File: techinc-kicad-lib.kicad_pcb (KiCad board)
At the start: 2 copper layers, 68.6 x 53.3 mm, 17 parts, among them IC1 WS2801, IC2 MAX490, IC3 WS2811, U1 ESP-01, U10 ARDUINOSHIELD, U11 ARDUINOSHIELD, U12 ARDUINOSHIELD, U13 IN-14, U2 ESP-03, U3 WS2812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

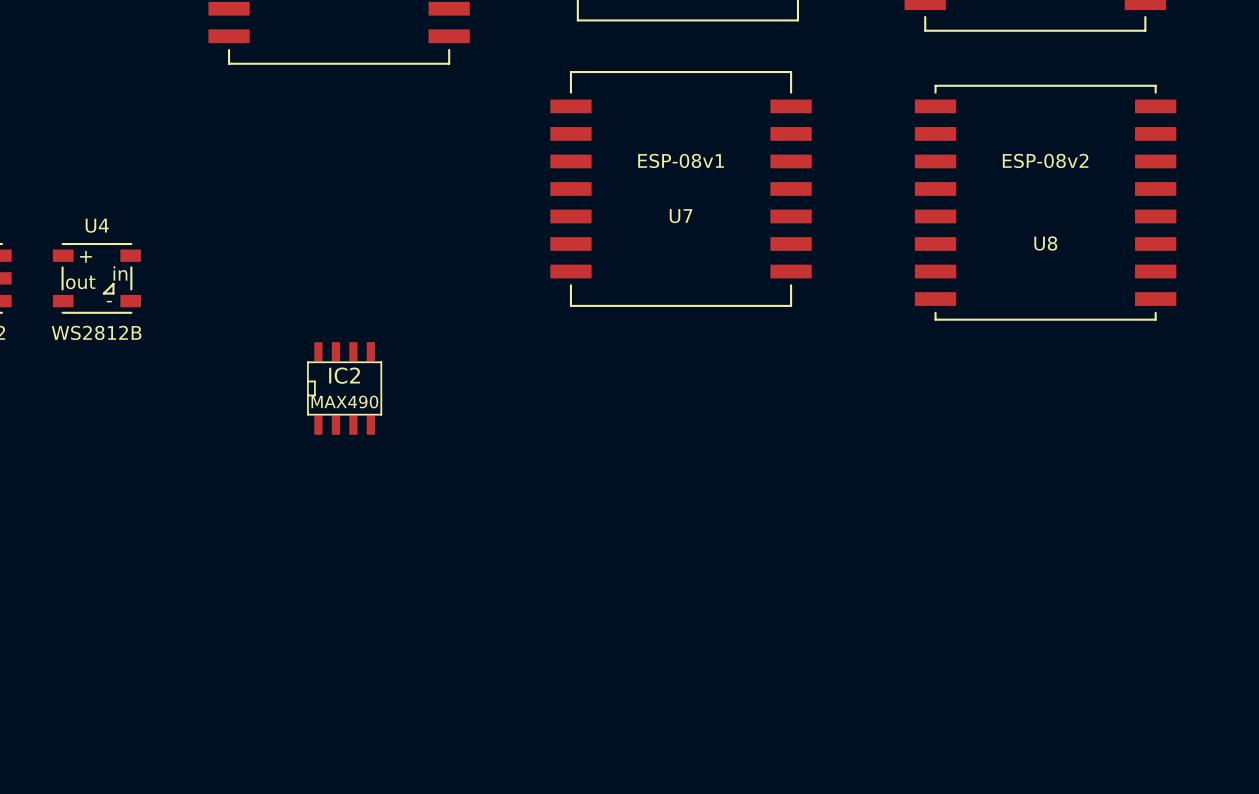
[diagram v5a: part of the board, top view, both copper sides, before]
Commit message: fix esp pinout, add SOT voltage regulator
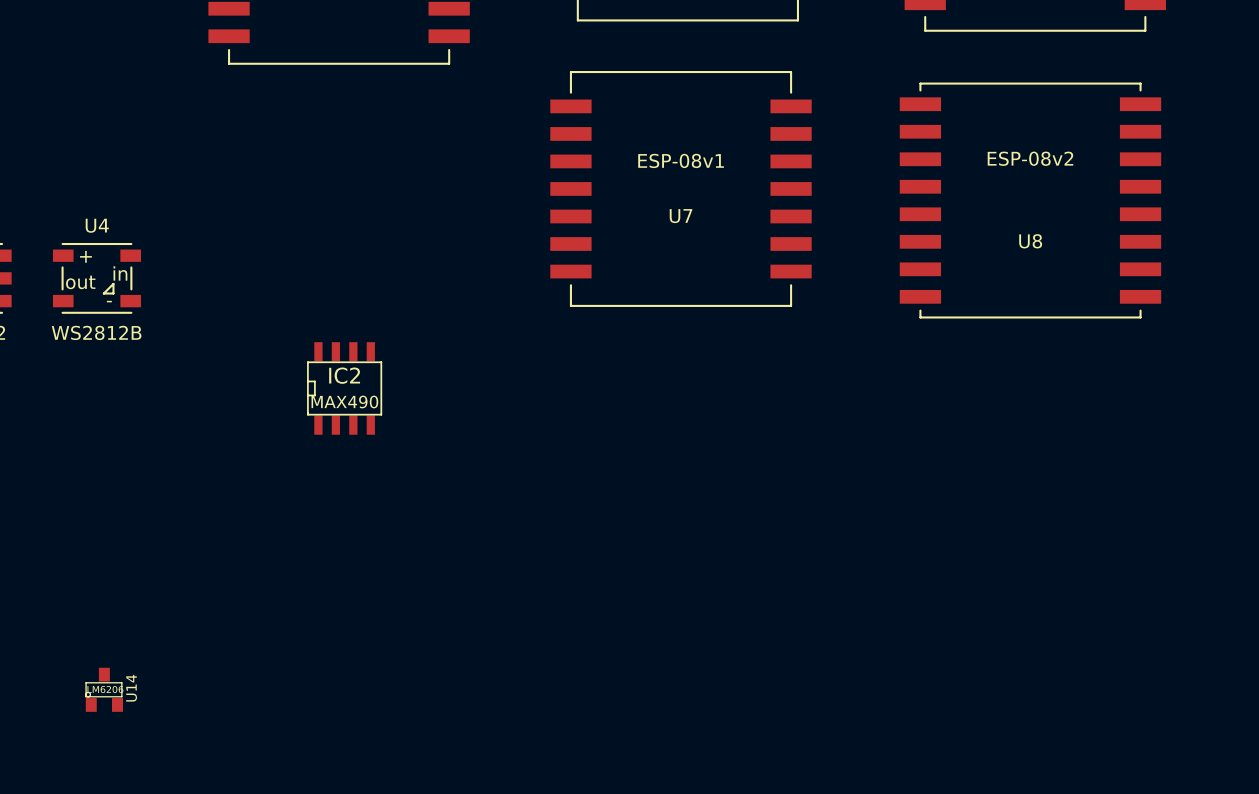
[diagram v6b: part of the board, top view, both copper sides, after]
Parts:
- added U14: LM6206, SOT23, F.Cu at (53.3, 88.9)
- moved U8 1.11 mm to (120.7, 53.3)
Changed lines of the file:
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@@
     (tracks 0)
     (zones 0)
-    (modules 17)
+    (modules 18)
     (nets 1)
   )
@@
     (mod_text_size 1 1)
     (mod_text_width 0.15)
-    (pad_size 1.5 1.5)
-    (pad_drill 1.016)
+    (pad_size 2 1)
+    (pad_drill 0)
     (pad_to_mask_clearance 0)
     (aux_axis_origin 0 0)
@@
     )
   )
-  (module ESP-08v2 (layer F.Cu)
-    (at 121.75 53.5)
-    (fp_text reference U8 (at 0 3) (layer F.SilkS)
-      (effects (font (size 1 1) (thickness 0.15)))
-    )
-    (fp_text value ESP-08v2 (at 0 -3) (layer F.SilkS)
-      (effects (font (size 1 1) (thickness 0.15)))
-    )
-    (fp_line (start -8 -8) (end -8 -8.5) (layer F.SilkS) (width 0.15))
-    (fp_line (start -8 -8.5) (end 8 -8.5) (layer F.SilkS) (width 0.15))
-    (fp_line (start 8 -8.5) (end 8 -8) (layer F.SilkS) (width 0.15))
-    (fp_line (start -8 8) (end -8 8.5) (layer F.SilkS) (width 0.15))
-    (fp_line (start -8 8.5) (end 8 8.5) (layer F.SilkS) (width 0.15))
-    (fp_line (start 8 8.5) (end 8 8) (layer F.SilkS) (width 0.15))
-    (pad 1 smd rect (at -8 -7) (size 3 1)
-      (layers F.Cu F.Paste F.Mask)
-    )
-    (pad 2 smd rect (at -8 -5) (size 3 1)
-      (layers F.Cu F.Paste F.Mask)
-    )
-    (pad 3 smd rect (at -8 -3) (size 3 1)
-      (layers F.Cu F.Paste F.Mask)
-    )
-    (pad 4 smd rect (at -8 -1) (size 3 1)
-      (layers F.Cu F.Paste F.Mask)
-    )
-    (pad 5 smd rect (at -8 1) (size 3 1)
-      (layers F.Cu F.Paste F.Mask)
-    )
-    (pad 6 smd rect (at -8 3) (size 3 1)
-      (layers F.Cu F.Paste F.Mask)
-    )
-    (pad 7 smd rect (at -8 5) (size 3 1)
-      (layers F.Cu F.Paste F.Mask)
-    )
-    (pad 8 smd rect (at -8 7) (size 3 1)
-      (layers F.Cu F.Paste F.Mask)
-    )
-    (pad 9 smd rect (at 8 7) (size 3 1)
-      (layers F.Cu F.Paste F.Mask)
-    )
-    (pad 10 smd rect (at 8 5) (size 3 1)
-      (layers F.Cu F.Paste F.Mask)
-    )
-    (pad 11 smd rect (at 8 3) (size 3 1)
-      (layers F.Cu F.Paste F.Mask)
-    )
-    (pad 12 smd rect (at 8 1) (size 3 1)
-      (layers F.Cu F.Paste F.Mask)
-    )
-    (pad 13 smd rect (at 8 -1) (size 3 1)
-      (layers F.Cu F.Paste F.Mask)
-    )
-    (pad 14 smd rect (at 8 -3) (size 3 1)
-      (layers F.Cu F.Paste F.Mask)
-    )
-    (pad 15 smd rect (at 8 -5) (size 3 1)
-      (layers F.Cu F.Paste F.Mask)
-    )
-    (pad 16 smd rect (at 8 -7) (size 3 1)
-      (layers F.Cu F.Paste F.Mask)
-    )
-  )
   (module ESP-08v1 (layer F.Cu)
     (at 95.25 52.5)
@@
     )
   )
+  (module ESP-08v2 (layer F.Cu)
+    (at 120.65 53.34)
+    (fp_text reference U8 (at 0 3) (layer F.SilkS)
+      (effects (font (size 1 1) (thickness 0.15)))
+    )
+    (fp_text value ESP-08v2 (at 0 -3) (layer F.SilkS)
+      (effects (font (size 1 1) (thickness 0.15)))
+    )
+    (fp_line (start -8 -8) (end -8 -8.5) (layer F.SilkS) (width 0.15))
+    (fp_line (start -8 -8.5) (end 8 -8.5) (layer F.SilkS) (width 0.15))
+    (fp_line (start 8 -8.5) (end 8 -8) (layer F.SilkS) (width 0.15))
+    (fp_line (start -8 8) (end -8 8.5) (layer F.SilkS) (width 0.15))
+    (fp_line (start -8 8.5) (end 8 8.5) (layer F.SilkS) (width 0.15))
+    (fp_line (start 8 8.5) (end 8 8) (layer F.SilkS) (width 0.15))
+    (pad 1 smd rect (at -8 -7) (size 3 1)
+      (layers F.Cu F.Paste F.Mask)
+    )
+    (pad 2 smd rect (at -8 -5) (size 3 1)
+      (layers F.Cu F.Paste F.Mask)
+    )
+    (pad 3 smd rect (at -8 -3) (size 3 1)
+      (layers F.Cu F.Paste F.Mask)
+    )
+    (pad 4 smd rect (at -8 -1) (size 3 1)
+      (layers F.Cu F.Paste F.Mask)
+    )
+    (pad 5 smd rect (at -8 1) (size 3 1)
+      (layers F.Cu F.Paste F.Mask)
+    )
+    (pad 6 smd rect (at -8 3) (size 3 1)
+      (layers F.Cu F.Paste F.Mask)
+    )
+    (pad 7 smd rect (at -8 5) (size 3 1)
+      (layers F.Cu F.Paste F.Mask)
+    )
+    (pad 8 smd rect (at -8 7) (size 3 1)
+      (layers F.Cu F.Paste F.Mask)
+    )
+    (pad 9 smd rect (at 8 7) (size 3 1)
+      (layers F.Cu F.Paste F.Mask)
+    )
+    (pad 10 smd rect (at 8 5) (size 3 1)
+      (layers F.Cu F.Paste F.Mask)
+    )
+    (pad 11 smd rect (at 8 3) (size 3 1)
+      (layers F.Cu F.Paste F.Mask)
+    )
+    (pad 12 smd rect (at 8 1) (size 3 1)
+      (layers F.Cu F.Paste F.Mask)
+    )
+    (pad 13 smd rect (at 8 -1) (size 3 1)
+      (layers F.Cu F.Paste F.Mask)
+    )
+    (pad 14 smd rect (at 8 -3) (size 3 1)
+      (layers F.Cu F.Paste F.Mask)
+    )
+    (pad 15 smd rect (at 8 -5) (size 3 1)
+      (layers F.Cu F.Paste F.Mask)
+    )
+    (pad 16 smd rect (at 8 -7) (size 3 1)
+      (layers F.Cu F.Paste F.Mask)
+    )
+  )
+  (module SOT23 (layer F.Cu)
+    (at 53.34 88.9)
+    (tags SOT23)
+    (fp_text reference U14 (at 1.99898 -0.09906 90) (layer F.SilkS)
+      (effects (font (size 0.762 0.762) (thickness 0.11938)))
+    )
+    (fp_text value LM6206 (at 0.0635 0) (layer F.SilkS)
+      (effects (font (size 0.50038 0.50038) (thickness 0.09906)))
+    )
+    (fp_circle (center -1.17602 0.35052) (end -1.30048 0.44958) (layer F.SilkS) (width 0.07874))
+    (fp_line (start 1.27 -0.508) (end 1.27 0.508) (layer F.SilkS) (width 0.07874))
+    (fp_line (start -1.3335 -0.508) (end -1.3335 0.508) (layer F.SilkS) (width 0.07874))
+    (fp_line (start 1.27 0.508) (end -1.3335 0.508) (layer F.SilkS) (width 0.07874))
+    (fp_line (start -1.3335 -0.508) (end 1.27 -0.508) (layer F.SilkS) (width 0.07874))
+    (pad 3 smd rect (at 0 -1.09982) (size 0.8001 1.00076)
+      (layers F.Cu F.Paste F.Mask)
+    )
+    (pad 2 smd rect (at 0.9525 1.09982) (size 0.8001 1.00076)
+      (layers F.Cu F.Paste F.Mask)
+    )
+    (pad 1 smd rect (at -0.9525 1.09982) (size 0.8001 1.00076)
+      (layers F.Cu F.Paste F.Mask)
+    )
+    (model smd\SOT23_3.wrl
+      (at (xyz 0 0 0))
+      (scale (xyz 0.4 0.4 0.4))
+      (rotate (xyz 0 0 180))
+    )
+  )
